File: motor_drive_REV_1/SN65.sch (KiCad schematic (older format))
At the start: 7 parts

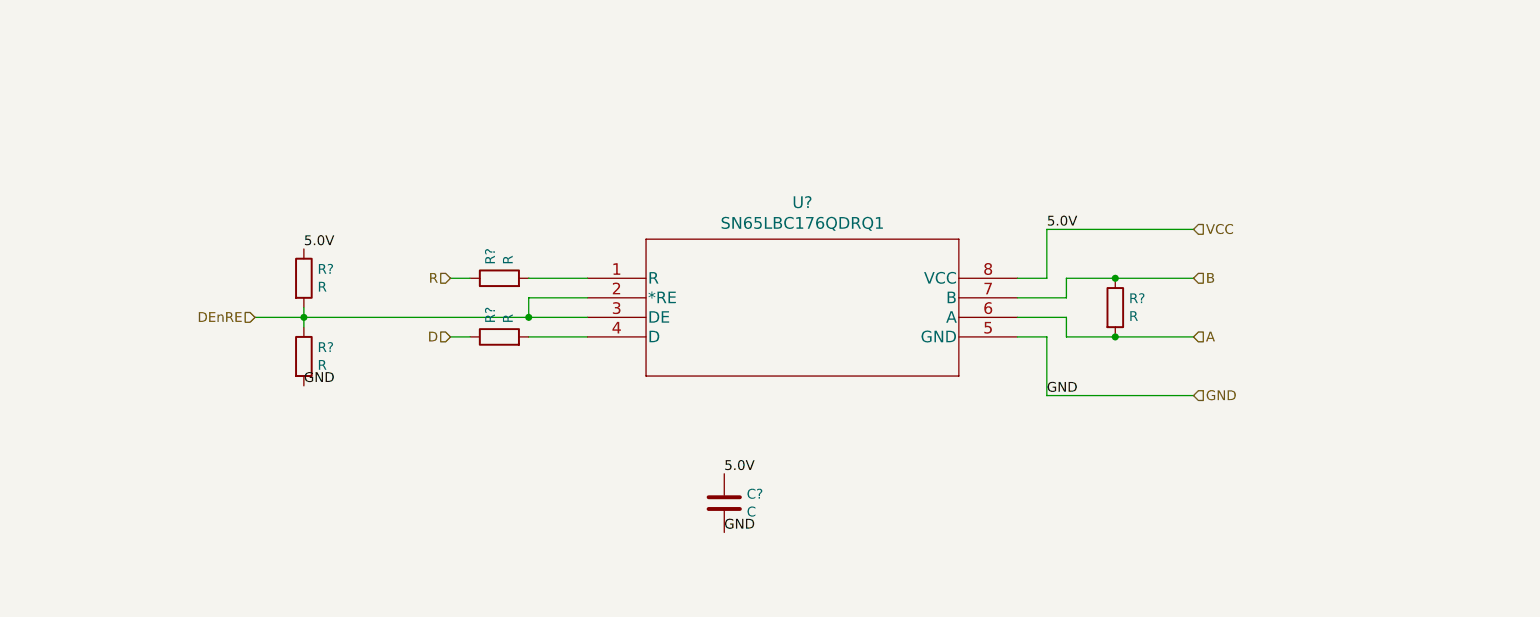
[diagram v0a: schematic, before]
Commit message: organizing pinout and BOM
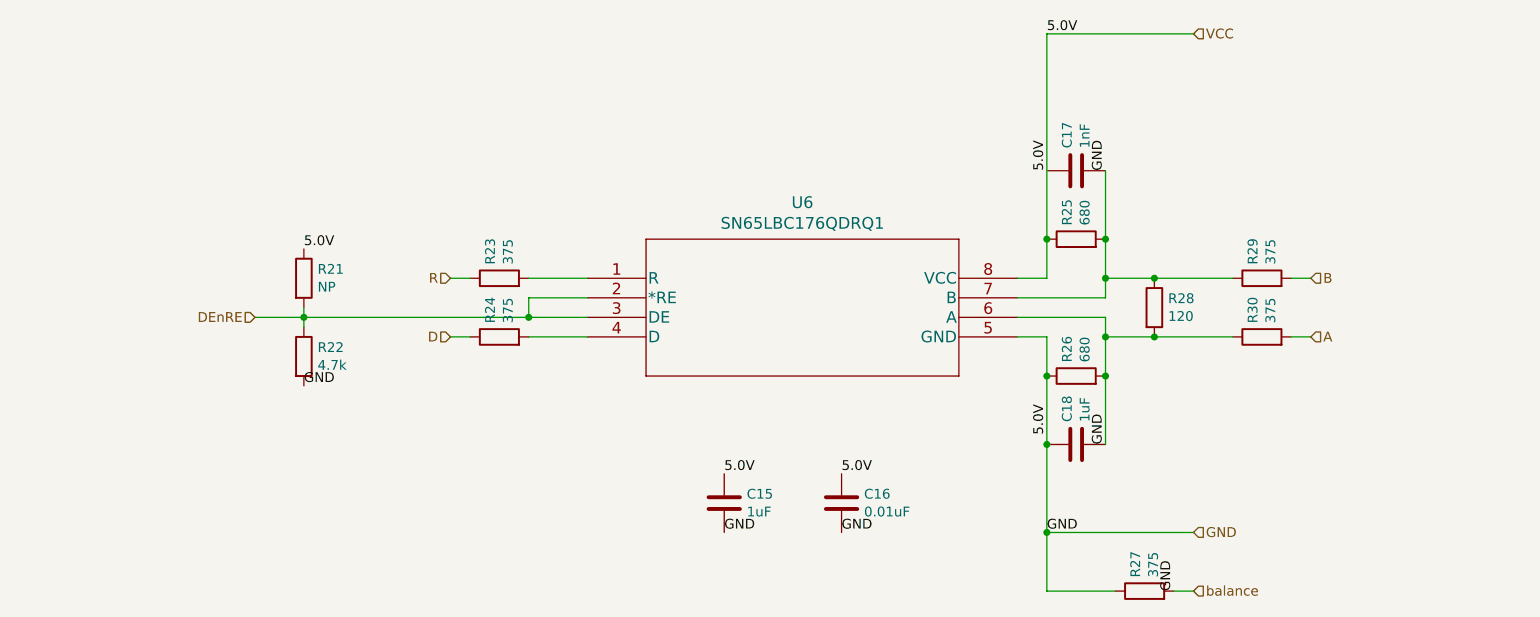
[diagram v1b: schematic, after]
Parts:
- added C16: 0.01uF, motor_drive_footprints:C_0603_1608Metric, symbol motor_drive:C
- added C17: 1nF, motor_drive_footprints:C_0603_1608Metric, symbol motor_drive:C
- added C18: 1uF, motor_drive_footprints:C_0603_1608Metric, symbol motor_drive:C
- added R25, R26: 680, motor_drive_footprints:C_0603_1608Metric, symbol motor_drive:R
- added R27, R29, R30: 375, motor_drive_footprints:C_0603_1608Metric, symbol motor_drive:R
- C15: renamed from C?; value C -> 1uF; footprint (none) -> motor_drive_footprints:C_0603_1608Metric
- R21: renamed from R?; value R -> NP; footprint (none) -> motor_drive_footprints:C_0603_1608Metric
- R22: renamed from R?; value R -> 4.7k; footprint (none) -> motor_drive_footprints:C_0603_1608Metric
- R23, R24: renamed from R?; value R -> 375; footprint (none) -> motor_drive_footprints:C_0603_1608Metric
- R28: renamed from R?; value R -> 120; footprint (none) -> motor_drive_footprints:C_0603_1608Metric
- U6: renamed from U?; footprint D8 -> motor_drive_footprints:SN65LBC176QDRQ1
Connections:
- net VCC is gone; now on net GND: C15.1, R21.1, U6.8 (VCC)
- net A: now also R30.2; no longer R28.2, U6.6 (A)
- net B: now also R29.2; no longer R28.1, U6.7 (B)
- net GND: now also R28.1, R28.2, U6.6 (A), U6.7 (B), C16.1, C16.2, C17.1, C17.2, C18.1, C18.2, R25.1, R25.2, R26.1, R26.2, R27.1, R27.2, R29.1, R30.1
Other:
- moved on the sheet: R28
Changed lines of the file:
@@
 $Descr A4 11693 8268
 encoding utf-8
-Sheet 14 14
+Sheet 11 14
 Title ""
 Date ""
@@
 Comment4 ""
 $EndDescr
-Text HLabel 7900 4100 2    50   Input ~ 0
+Text HLabel 7900 4800 2    50   Input ~ 0
 GND
 Wire Wire Line
 	7000 3800 7150 3800
-Wire Wire Line
-	7150 3800 7150 4100
-Text HLabel 7900 3250 2    50   Input ~ 0
+Text HLabel 7900 2250 2    50   Input ~ 0
 VCC
 Wire Wire Line
@@
 	4500 3600 4500 3700
 Wire Wire Line
-	7150 4100 7900 4100
-Wire Wire Line
-	7900 3250 7150 3250
-Wire Wire Line
-	7150 3250 7150 3500
-$Comp
-L motor_drive:R R?
+	7150 4800 7900 4800
+Wire Wire Line
+	7900 2250 7150 2250
+$Comp
+L motor_drive:R R21
 U 1 1 5E39658B
 P 3350 3500
-F 0 "R?" H 3420 3546 50  0000 L CNN
-F 1 "R" H 3420 3455 50  0000 L CNN
-F 2 "" V 3280 3500 50  0001 C CNN
+F 0 "R21" H 3420 3546 50  0000 L CNN
+F 1 "NP" H 3420 3455 50  0000 L CNN
+F 2 "motor_drive_footprints:C_0603_1608Metric" V 3280 3500 50  0001 C CNN
 F 3 "~" H 3350 3500 50  0001 C CNN
 	1    3350 3500
@@
 Connection ~ 3350 3700
 Wire Wire Line
-	7250 3800 7500 3800
-Wire Wire Line
-	7250 3500 7500 3500
-Wire Wire Line
-	7500 3800 7900 3800
-Connection ~ 7500 3800
-Wire Wire Line
-	7500 3500 7900 3500
-Connection ~ 7500 3500
-Text HLabel 7900 3800 2    50   Input ~ 0
-A
-Text HLabel 7900 3500 2    50   Input ~ 0
-B
-Wire Wire Line
-	7250 3700 7250 3800
-Wire Wire Line
-	7000 3700 7250 3700
-Wire Wire Line
-	7250 3600 7250 3500
-Wire Wire Line
-	7000 3600 7250 3600
-$Comp
-L motor_drive:R R?
-U 1 1 5E390D6F
-P 7500 3650
-F 0 "R?" H 7570 3696 50  0000 L CNN
-F 1 "R" H 7570 3605 50  0000 L CNN
-F 2 "" V 7430 3650 50  0001 C CNN
-F 3 "~" H 7500 3650 50  0001 C CNN
-	1    7500 3650
-	1    0    0    -1
-$EndComp
-Wire Wire Line
 	3350 3700 3350 3750
 $Comp
-L motor_drive:C C?
+L motor_drive:C C15
 U 1 1 5E39B417
 P 5500 4650
-F 0 "C?" H 5615 4696 50  0000 L CNN
-F 1 "C" H 5615 4605 50  0000 L CNN
-F 2 "" H 5538 4500 50  0001 C CNN
+F 0 "C15" H 5615 4696 50  0000 L CNN
+F 1 "1uF" H 5615 4605 50  0000 L CNN
+F 2 "motor_drive_footprints:C_0603_1608Metric" H 5538 4500 50  0001 C CNN
 F 3 "~" H 5500 4650 50  0001 C CNN
 	1    5500 4650
@@
 $EndComp
 $Comp
-L motor_drive:SN65LBC176QDRQ1 U?
+L motor_drive:SN65LBC176QDRQ1 U6
 U 1 1 5E3956B5
 P 4800 3500
-F 0 "U?" H 5900 3887 60  0000 C CNN
+F 0 "U6" H 5900 3887 60  0000 C CNN
 F 1 "SN65LBC176QDRQ1" H 5900 3781 60  0000 C CNN
-F 2 "D8" H 5900 3740 60  0001 C CNN
+F 2 "motor_drive_footprints:SN65LBC176QDRQ1" H 5900 3740 60  0001 C CNN
 F 3 "" H 4800 3500 60  0000 C CNN
 	1    4800 3500
@@
 GND
 $Comp
-L motor_drive:R R?
+L motor_drive:R R22
 U 1 1 5E39AB4E
 P 3350 3900
-F 0 "R?" H 3420 3946 50  0000 L CNN
-F 1 "R" H 3420 3855 50  0000 L CNN
-F 2 "" V 3280 3900 50  0001 C CNN
+F 0 "R22" H 3420 3946 50  0000 L CNN
+F 1 "4.7k" H 3420 3855 50  0000 L CNN
+F 2 "motor_drive_footprints:C_0603_1608Metric" V 3280 3900 50  0001 C CNN
 F 3 "~" H 3350 3900 50  0001 C CNN
 	1    3350 3900
 	1    0    0    -1
 $EndComp
-Text Label 7150 3250 0    50   ~ 0
-5.0V
-Text Label 7150 4100 0    50   ~ 0
+Text Label 7150 2250 0    50   ~ 0
+5.0V
+Text Label 7150 4800 0    50   ~ 0
 GND
 Text Label 3350 3350 0    50   ~ 0
@@
 GND
 $Comp
-L motor_drive:R R?
+L motor_drive:R R23
 U 1 1 5E3A24BE
 P 4350 3500
-F 0 "R?" H 4420 3546 50  0000 L CNN
-F 1 "R" H 4420 3455 50  0000 L CNN
-F 2 "" V 4280 3500 50  0001 C CNN
+F 0 "R23" H 4420 3546 50  0000 L CNN
+F 1 "375" H 4420 3455 50  0000 L CNN
+F 2 "motor_drive_footprints:C_0603_1608Metric" V 4280 3500 50  0001 C CNN
 F 3 "~" H 4350 3500 50  0001 C CNN
 	1    4350 3500
@@
 $EndComp
 $Comp
-L motor_drive:R R?
+L motor_drive:R R24
 U 1 1 5E3A2A5B
 P 4350 3800
-F 0 "R?" H 4420 3846 50  0000 L CNN
-F 1 "R" H 4420 3755 50  0000 L CNN
-F 2 "" V 4280 3800 50  0001 C CNN
+F 0 "R24" H 4420 3846 50  0000 L CNN
+F 1 "375" H 4420 3755 50  0000 L CNN
+F 2 "motor_drive_footprints:C_0603_1608Metric" V 4280 3800 50  0001 C CNN
 F 3 "~" H 4350 3800 50  0001 C CNN
 	1    4350 3800
@@
 Wire Wire Line
 	4500 3800 4800 3800
+$Comp
+L motor_drive:R R27
+U 1 1 5E33ED83
+P 7650 5100
+F 0 "R27" H 7720 5146 50  0000 L CNN
+F 1 "375" H 7720 5055 50  0000 L CNN
+F 2 "motor_drive_footprints:C_0603_1608Metric" V 7580 5100 50  0001 C CNN
+F 3 "~" H 7650 5100 50  0001 C CNN
+	1    7650 5100
+	0    -1   -1   0
+$EndComp
+Text Label 7800 5100 1    50   ~ 0
+GND
+Text HLabel 7900 5100 2    50   Input ~ 0
+balance
+Wire Wire Line
+	7800 5100 7900 5100
+Wire Wire Line
+	7500 5100 7150 5100
+Wire Wire Line
+	7150 5100 7150 4800
+Connection ~ 7150 4800
+$Comp
+L motor_drive:R R28
+U 1 1 5E390D6F
+P 7700 3650
+F 0 "R28" H 7770 3696 50  0000 L CNN
+F 1 "120" H 7770 3605 50  0000 L CNN
+F 2 "motor_drive_footprints:C_0603_1608Metric" V 7630 3650 50  0001 C CNN
+F 3 "~" H 7700 3650 50  0001 C CNN
+	1    7700 3650
+	1    0    0    -1
+$EndComp
+Wire Wire Line
+	7450 3700 7450 3800
+Text HLabel 8500 3500 2    50   Input ~ 0
+B
+Text HLabel 8500 3800 2    50   Input ~ 0
+A
+Wire Wire Line
+	7700 3500 8100 3500
+Connection ~ 7700 3800
+Wire Wire Line
+	7700 3800 8100 3800
+Wire Wire Line
+	7450 3800 7700 3800
+$Comp
+L motor_drive:R R26
+U 1 1 5E37C57B
+P 7300 4000
+F 0 "R26" H 7370 4046 50  0000 L CNN
+F 1 "680" H 7370 3955 50  0000 L CNN
+F 2 "motor_drive_footprints:C_0603_1608Metric" V 7230 4000 50  0001 C CNN
+F 3 "~" H 7300 4000 50  0001 C CNN
+	1    7300 4000
+	0    -1   -1   0
+$EndComp
+$Comp
+L motor_drive:R R25
+U 1 1 5E37CBBC
+P 7300 3300
+F 0 "R25" H 7370 3346 50  0000 L CNN
+F 1 "680" H 7370 3255 50  0000 L CNN
+F 2 "motor_drive_footprints:C_0603_1608Metric" V 7230 3300 50  0001 C CNN
+F 3 "~" H 7300 3300 50  0001 C CNN
+	1    7300 3300
+	0    -1   -1   0
+$EndComp
+Wire Wire Line
+	7000 3600 7450 3600
+Wire Wire Line
+	7000 3700 7450 3700
+$Comp
+L motor_drive:R R29
+U 1 1 5E37EDA8
+P 8250 3500
+F 0 "R29" H 8320 3546 50  0000 L CNN
+F 1 "375" H 8320 3455 50  0000 L CNN
+F 2 "motor_drive_footprints:C_0603_1608Metric" V 8180 3500 50  0001 C CNN
+F 3 "~" H 8250 3500 50  0001 C CNN
+	1    8250 3500
+	0    -1   -1   0
+$EndComp
+$Comp
+L motor_drive:R R30
+U 1 1 5E37F275
+P 8250 3800
+F 0 "R30" H 8320 3846 50  0000 L CNN
+F 1 "375" H 8320 3755 50  0000 L CNN
+F 2 "motor_drive_footprints:C_0603_1608Metric" V 8180 3800 50  0001 C CNN
+F 3 "~" H 8250 3800 50  0001 C CNN
+	1    8250 3800
+	0    -1   -1   0
+$EndComp
+Wire Wire Line
+	8400 3500 8500 3500
+Wire Wire Line
+	8400 3800 8500 3800
+Wire Wire Line
+	7150 3800 7150 4000
+Wire Wire Line
+	7150 2250 7150 3300
+Connection ~ 7150 4000
+Wire Wire Line
+	7150 4000 7150 4350
+Connection ~ 7150 3300
+Wire Wire Line
+	7150 3300 7150 3500
+$Comp
+L motor_drive:C C18
+U 1 1 5E386871
+P 7300 4350
+F 0 "C18" H 7415 4396 50  0000 L CNN
+F 1 "1uF" H 7415 4305 50  0000 L CNN
+F 2 "motor_drive_footprints:C_0603_1608Metric" H 7338 4200 50  0001 C CNN
+F 3 "~" H 7300 4350 50  0001 C CNN
+	1    7300 4350
+	0    -1   -1   0
+$EndComp
+Text Label 7150 4300 1    50   ~ 0
+5.0V
+Text Label 7450 4350 1    50   ~ 0
+GND
+$Comp
+L motor_drive:C C17
+U 1 1 5E387278
+P 7300 2950
+F 0 "C17" H 7415 2996 50  0000 L CNN
+F 1 "1nF" H 7415 2905 50  0000 L CNN
+F 2 "motor_drive_footprints:C_0603_1608Metric" H 7338 2800 50  0001 C CNN
+F 3 "~" H 7300 2950 50  0001 C CNN
+	1    7300 2950
+	0    -1   -1   0
+$EndComp
+Text Label 7150 2950 1    50   ~ 0
+5.0V
+Text Label 7450 2950 1    50   ~ 0
+GND
+Wire Wire Line
+	7450 3800 7450 4000
+Connection ~ 7450 3800
+Wire Wire Line
+	7450 3600 7450 3500
+Wire Wire Line
+	7450 3300 7450 2950
+Connection ~ 7450 3300
+Connection ~ 7150 4350
+Wire Wire Line
+	7150 4350 7150 4800
+Wire Wire Line
+	7450 4000 7450 4350
+Connection ~ 7450 4000
+Wire Wire Line
+	7700 3500 7450 3500
+Connection ~ 7700 3500
+Connection ~ 7450 3500
+Wire Wire Line
+	7450 3500 7450 3300
+$Comp
+L motor_drive:C C16
+U 1 1 5E3AD083
+P 6100 4650
+F 0 "C16" H 6215 4696 50  0000 L CNN
+F 1 "0.01uF" H 6215 4605 50  0000 L CNN
+F 2 "motor_drive_footprints:C_0603_1608Metric" H 6138 4500 50  0001 C CNN
+F 3 "~" H 6100 4650 50  0001 C CNN
+	1    6100 4650
+	1    0    0    -1
+$EndComp
+Text Label 6100 4500 0    50   ~ 0
+5.0V
+Text Label 6100 4800 0    50   ~ 0
+GND
 $EndSCHEMATC
